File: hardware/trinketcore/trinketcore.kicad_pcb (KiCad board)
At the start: 4 copper layers, 40 x 60 mm, 115 parts, among them J1 USB-C, J4 DISPLAY, J5 I2C OLED, J6 EXPANSION, J7 SPEAKER, J8 QWIIC, Q1 AO3401A, Q2 AO3400A, Q3 AO3400A, Q4 AO3400A, Q5 AO3401A, Q6 AO3400A, Q7 AO3401A, Q8 AO3400A, Q9 AO3400A, SW1 POWER/A, SW2 B, SW3 BOOT, SW4 RESET, U1 USBLC6-2SC6, U2 BQ25173DSGR, U3 TPS3808G01DBVR, U4 TPS63031DSKR, U5 PCF8563T, U6 RP2040, U7 W25Q128JVS, U8 MAX98357A, Y1 32.768kHz, Y2 12MHz

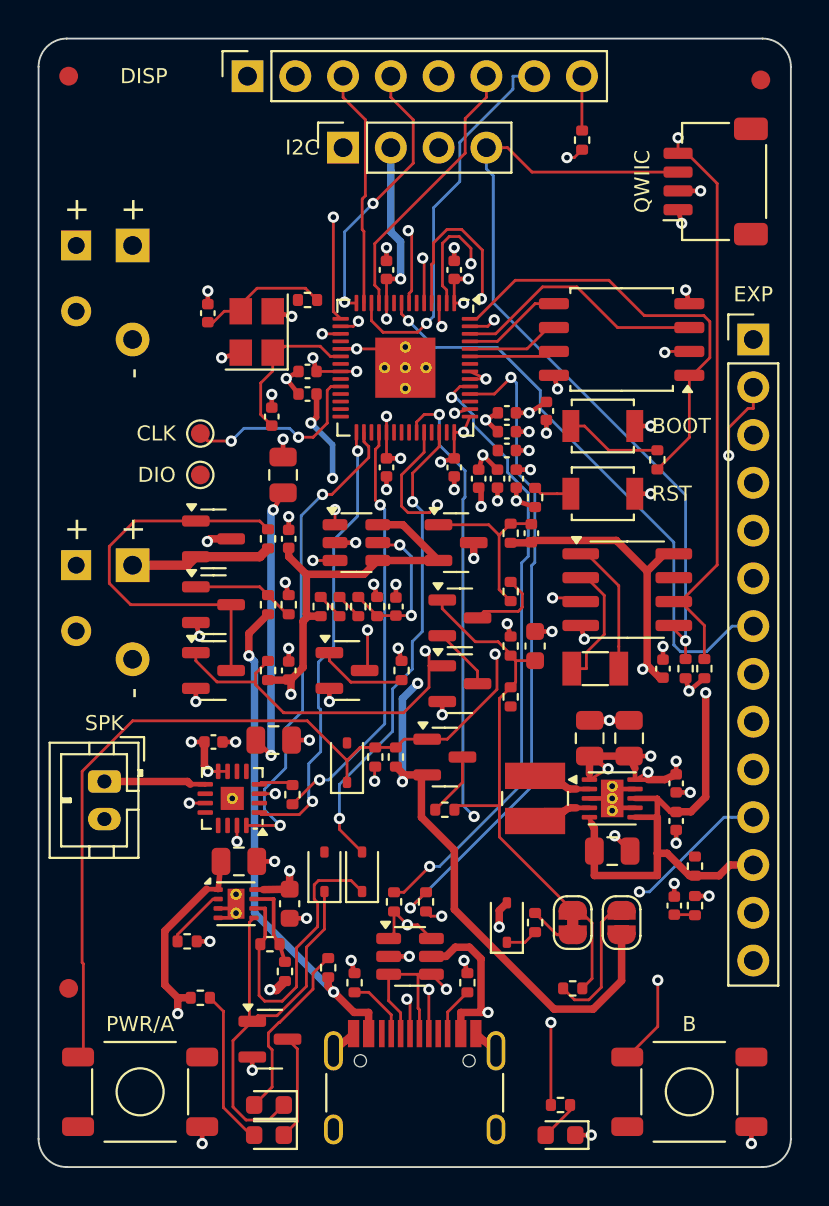
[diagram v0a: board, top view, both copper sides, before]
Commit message: TrinketCore: pin map that routes without crossings (work in progress)
The first autoroute left four connections open. Three of them were at the
RP2040, where the expansion header took GP0..GP7 in the opposite order to the
chip's pins, and USB_DET had to cross GP26/GP27 on the bottom row. The fourth
was the speaker output, hemmed in by a ground via.

- J6 now runs GP7..GP0, GP29, GP28 (pin 1 at the top), matching the pin order.
- Bottom row: CHG GP22, button A GP23, USB_DET GP24, user LED GP25 (unchanged),
  HOLD GP26, VSENSE GP27, J6 analog GP28/GP29. Display DC/CS swap to GP9/GP8.
- The amplifier's ground pins tie into its exposed pad instead of vias, and the
  RP2040 decoupling capacitors share their pins' plane vias.
- route_pcb.py runs a second Freerouting pass on the first pass's result, and
  the grid router falls back to 0.15 mm tracks.

Firmware and docs follow the new pin map. The board is being re-routed; the
board file in this commit is not routed yet.

Co-Authored-By: Claude Opus 5.5 <noreply@anthropic.com>
Claude-Session: https://claude.ai/code/session_01V89YvrQurcttiFbkgcTPH9
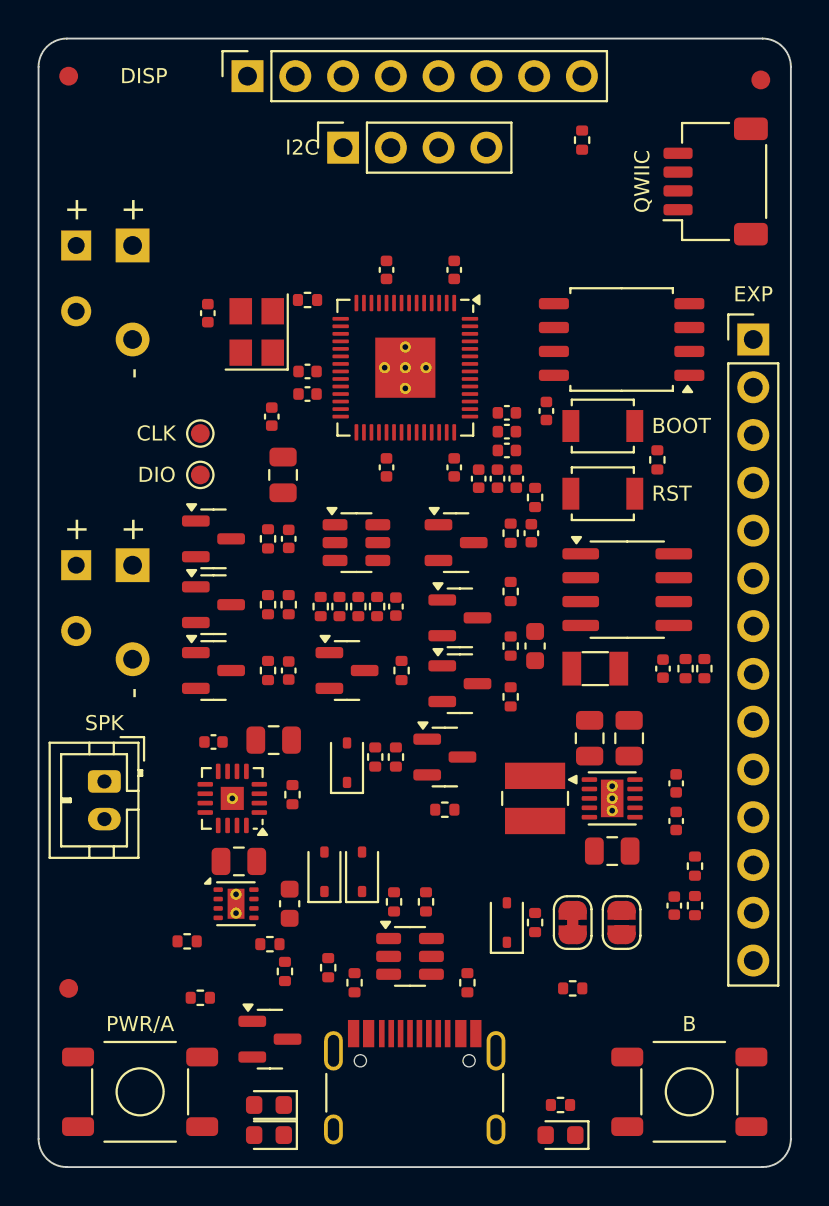
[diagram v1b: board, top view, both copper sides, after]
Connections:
- J6 pad 1: GP0 -> GP7
- J6 pad 10: GP27 -> GP28
- J6 pad 2: GP1 -> GP6
- J6 pad 3: GP2 -> GP5
- J6 pad 4: GP3 -> GP4
- J6 pad 5: GP4 -> GP3
- J6 pad 6: GP5 -> GP2
- J6 pad 7: GP6 -> GP1
- J6 pad 8: GP7 -> GP0
- J6 pad 9: GP26 -> GP29
- U6 pad 11: TFT_DC -> TFT_CS
- U6 pad 12: TFT_CS -> TFT_DC
- U6 pad 34: HOLD -> CHG
- U6 pad 36: CHG -> USB_DET
- U6 pad 38: GP26 -> HOLD
- U6 pad 39: GP27 -> VSENSE
- U6 pad 40: USB_DET -> GP28
- U6 pad 41: VSENSE -> GP29
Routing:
- net 3V3: track 166.3 -> 0.00 mm, vias 27 -> 0
- net VAON: track 99.3 -> 0.00 mm, vias 5 -> 0
- net BTN_B: track 70.1 -> 0.00 mm, vias 2 -> 0
- net VBUS: track 69.6 -> 0.00 mm, vias 5 -> 0
- net VCAP: track 62.6 -> 0.00 mm, vias 2 -> 0
- net GND: track 59.4 -> 0.00 mm, vias 56 -> 0
- net WAKE_N: track 49.9 -> 0.00 mm, vias 2 -> 0
- net GP5: track 44.3 -> 0.00 mm, vias 1 -> 0
- net SCL: track 44.2 -> 0.00 mm, vias 1 -> 0
- net VSYS: track 43.9 -> 0.00 mm, vias 2 -> 0
- net SDA: track 43.4 -> 0.00 mm, vias 1 -> 0
- net USER_LED: track 41.2 -> 0.00 mm, vias 3 -> 0
- net GP3: track 37.5 -> 0.00 mm, vias 1 -> 0
- net USB_DM: track 35.2 -> 0.00 mm, vias 2 -> 0
- net GP26: track 34.1 -> 0.00 mm, vias 1 -> 0
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- removed copper zone on In1.Cu, net GND
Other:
- board text added: "GP28"
- board text added: "GP29"
- board text removed: "GP26"
- board text removed: "GP27"

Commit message: Add e-ink tarot oracle; routing fixes (work in progress)
- firmware/trinketcore/circuitpython/oracle: each press draws a random tarot
  card on a 1.54" SSD1681 e-paper module with a charge icon, then switches the
  board off (the card stays on screen with no power). make_cards.py turns card
  art into dithered 1-bit or black/white/red BMPs with the card's name.
- trinketcore.EPD_BUSY: e-paper BUSY reads on J4's BLK pin (GP13).
- READMEs and the design-method guide cover e-ink wiring and runtimes.
- route_pcb.py: the finisher now sees open connections at SMD pads (the
  report parser only matched "PTH pad"), rips up tracks around boxed-in pads
  and routes them first, and 1V1 uses the default 0.15 mm width so it fits
  between the RP2040's pins. Same parser fix in CapCore's script.
- The SWD test pads are gone (the USB bootloader is in ROM).

The board is being re-routed; the board file in this commit is not routed.

Co-Authored-By: Claude Opus 5.5 <noreply@anthropic.com>
Claude-Session: https://claude.ai/code/session_01V89YvrQurcttiFbkgcTPH9
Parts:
- removed TP1: SWCLK, TestPoint:TestPoint_Pad_D1.0mm
- removed TP2: SWDIO, TestPoint:TestPoint_Pad_D1.0mm
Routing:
- net GND: track 0.00 -> 59.1 mm, vias 0 -> 53
- net 3V3: track 0.00 -> 38.5 mm, vias 0 -> 22
- net VSYS: track 0.00 -> 14.3 mm
- net FB: track 0.00 -> 4.53 mm
- net VCAP: track 0.00 -> 2.88 mm, vias 0 -> 1
- net PG_N: track 0.00 -> 2.59 mm
- net LX2: track 0.00 -> 1.81 mm
- net LX1: track 0.00 -> 1.81 mm
- net VBUS: track 0.00 -> 1.51 mm
- added copper zone on In2.Cu, net 3V3
- added copper zone on B.Cu, net GND
- added copper zone on F.Cu, net GND
- added copper zone on In1.Cu, net GND
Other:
- board text removed: "CLK"
- board text removed: "DIO"

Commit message: TrinketCore: second-pass autoroute session (work in progress)
The grid-router finish, pours and checks follow.

Co-Authored-By: Claude Opus 5.5 <noreply@anthropic.com>
Claude-Session: https://claude.ai/code/session_01V89YvrQurcttiFbkgcTPH9
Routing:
- net 3V3: track 38.5 -> 169.9 mm
- net VAON: track 0.00 -> 91.1 mm, vias 0 -> 6
- net SDA: track 0.00 -> 67.0 mm, vias 0 -> 2
- net VBUS: track 1.51 -> 64.8 mm, vias 0 -> 4
- net SCL: track 0.00 -> 62.5 mm, vias 0 -> 2
- net VCAP: track 2.88 -> 62.7 mm, vias 1 -> 2
- net WAKE_N: track 0.00 -> 51.9 mm, vias 0 -> 4
- net BTN_B: track 0.00 -> 51.6 mm, vias 0 -> 4
- net 1V1: track 0.00 -> 49.1 mm, vias 0 -> 7
- net USER_LED: track 0.00 -> 42.4 mm, vias 0 -> 2
- net USB_DM: track 0.00 -> 39.9 mm, vias 0 -> 2
- net USB_DP: track 0.00 -> 39.9 mm, vias 0 -> 2
- net GP2: track 0.00 -> 37.5 mm, vias 0 -> 1
- net VSENSE: track 0.00 -> 34.7 mm, vias 0 -> 4
- net VSYS: track 14.3 -> 48.4 mm, vias 0 -> 1
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- removed copper zone on In2.Cu, net 3V3
- removed copper zone on B.Cu, net GND
- removed copper zone on F.Cu, net GND

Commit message: TrinketCore: hand-routed crystal corner (work in progress)
The crystal's 1 k resistor now faces the crystal, the XIN capacitor turns so
its signal pad faces the crystal, and pin 22's capacitor moves onto the 3V3
plane to clear the way. XIN and XO are drawn by hand on F.Cu and XOUT hops
over XIN on In2.Cu, so the autorouter no longer has to untangle them.
The board is being re-routed.

Co-Authored-By: Claude Opus 5.5 <noreply@anthropic.com>
Claude-Session: https://claude.ai/code/session_01V89YvrQurcttiFbkgcTPH9
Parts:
- moved C20 6.22 mm to (9.30, 21.4), turned to 90 degrees
- turned C16 to -90 degrees
- turned R31 to 180 degrees
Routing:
- net 3V3: track 169.9 -> 37.9 mm, vias 22 -> 23
- net VAON: track 91.1 -> 0.00 mm, vias 6 -> 0
- net SDA: track 67.0 -> 0.00 mm, vias 2 -> 0
- net VBUS: track 64.8 -> 1.51 mm, vias 4 -> 0
- net SCL: track 62.5 -> 0.00 mm, vias 2 -> 0
- net VCAP: track 62.7 -> 2.88 mm, vias 2 -> 1
- net WAKE_N: track 51.9 -> 0.00 mm, vias 4 -> 0
- net BTN_B: track 51.6 -> 0.00 mm, vias 4 -> 0
- net 1V1: track 49.1 -> 0.00 mm, vias 7 -> 0
- net USER_LED: track 42.4 -> 0.00 mm, vias 2 -> 0
- net USB_DM: track 39.9 -> 0.00 mm, vias 2 -> 0
- net USB_DP: track 39.9 -> 0.00 mm, vias 2 -> 0
- net GP2: track 37.5 -> 0.00 mm, vias 1 -> 0
- net VSENSE: track 34.7 -> 0.00 mm, vias 4 -> 0
- net VSYS: track 48.4 -> 14.3 mm, vias 1 -> 0
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- added copper zone on In2.Cu, net 3V3
- added copper zone on B.Cu, net GND
- added copper zone on F.Cu, net GND

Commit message: TrinketCore: second-pass session for the new crystal corner (work in progress)
Co-Authored-By: Claude Opus 5.5 <noreply@anthropic.com>
Claude-Session: https://claude.ai/code/session_01V89YvrQurcttiFbkgcTPH9
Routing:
- net 3V3: track 37.9 -> 168.2 mm
- net VAON: track 0.00 -> 94.2 mm, vias 0 -> 4
- net BTN_B: track 0.00 -> 66.5 mm, vias 0 -> 3
- net SCL: track 0.00 -> 64.1 mm, vias 0 -> 2
- net SDA: track 0.00 -> 60.8 mm, vias 0 -> 4
- net WAKE_N: track 0.00 -> 59.8 mm, vias 0 -> 3
- net VCAP: track 2.88 -> 61.3 mm, vias 1 -> 2
- net VBUS: track 1.51 -> 56.9 mm, vias 0 -> 6
- net UVLO_OK: track 0.00 -> 42.2 mm, vias 0 -> 2
- net USER_LED: track 0.00 -> 40.0 mm, vias 0 -> 2
- net VSENSE: track 0.00 -> 35.8 mm, vias 0 -> 2
- net VSYS: track 14.3 -> 48.1 mm, vias 0 -> 1
- net GP28: track 0.00 -> 30.9 mm, vias 0 -> 1
- net GP2: track 0.00 -> 30.4 mm, vias 0 -> 1
- net EN_SYS: track 0.00 -> 29.9 mm
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- removed copper zone on In2.Cu, net 3V3
- removed copper zone on B.Cu, net GND
- removed copper zone on F.Cu, net GND

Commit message: TrinketCore: free the RP2040's top escape lanes (work in progress)
C18 and C19, the decoupling capacitors for pins 1 and 10, move to the
chip's corners on their own plane vias, so the GPIO and display tracks can
leave the top row in parallel. The second Freerouting pass gets 40 passes
and the grid router a wider rip-up radius. The board is being re-routed.

Co-Authored-By: Claude Opus 5.5 <noreply@anthropic.com>
Claude-Session: https://claude.ai/code/session_01V89YvrQurcttiFbkgcTPH9
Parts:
- moved C19 3.37 mm to (15.2, 11.6)
- moved C18 1.71 mm to (23.7, 12.9), turned to 0 degrees
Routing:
- net 3V3: track 168.2 -> 36.7 mm, vias 23 -> 25
- net VAON: track 94.2 -> 0.00 mm, vias 4 -> 0
- net BTN_B: track 66.5 -> 0.00 mm, vias 3 -> 0
- net SCL: track 64.1 -> 0.00 mm, vias 2 -> 0
- net SDA: track 60.8 -> 0.00 mm, vias 4 -> 0
- net WAKE_N: track 59.8 -> 0.00 mm, vias 3 -> 0
- net VCAP: track 61.3 -> 2.88 mm, vias 2 -> 1
- net VBUS: track 56.9 -> 1.51 mm, vias 6 -> 0
- net UVLO_OK: track 42.2 -> 0.00 mm, vias 2 -> 0
- net USER_LED: track 40.0 -> 0.00 mm, vias 2 -> 0
- net VSENSE: track 35.8 -> 0.00 mm, vias 2 -> 0
- net VSYS: track 48.1 -> 14.3 mm, vias 1 -> 0
- net GP28: track 30.9 -> 0.00 mm, vias 1 -> 0
- net GP2: track 30.4 -> 0.00 mm, vias 1 -> 0
- net EN_SYS: track 29.9 -> 0.00 mm
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- added copper zone on In2.Cu, net 3V3
- added copper zone on B.Cu, net GND
- added copper zone on F.Cu, net GND

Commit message: TrinketCore: second-pass session, free escape lanes (work in progress)
Co-Authored-By: Claude Opus 5.5 <noreply@anthropic.com>
Claude-Session: https://claude.ai/code/session_01V89YvrQurcttiFbkgcTPH9
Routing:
- net 3V3: track 36.7 -> 167.7 mm
- net VAON: track 0.00 -> 109.1 mm, vias 0 -> 5
- net SDA: track 0.00 -> 66.6 mm, vias 0 -> 3
- net SCL: track 0.00 -> 62.7 mm, vias 0 -> 2
- net VBUS: track 1.51 -> 63.7 mm, vias 0 -> 4
- net VCAP: track 2.88 -> 62.7 mm, vias 1 -> 2
- net BTN_B: track 0.00 -> 51.8 mm, vias 0 -> 3
- net 1V1: track 0.00 -> 47.9 mm, vias 0 -> 6
- net USER_LED: track 0.00 -> 46.4 mm, vias 0 -> 3
- net CHG: track 0.00 -> 44.8 mm, vias 0 -> 2
- net WAKE_N: track 0.00 -> 41.7 mm, vias 0 -> 4
- net USB_DP: track 0.00 -> 37.9 mm, vias 0 -> 2
- net VSENSE: track 0.00 -> 35.9 mm, vias 0 -> 2
- net I2S_BCLK: track 0.00 -> 34.6 mm, vias 0 -> 3
- net GP28: track 0.00 -> 33.4 mm, vias 0 -> 2
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- removed copper zone on In2.Cu, net 3V3
- removed copper zone on B.Cu, net GND
- removed copper zone on F.Cu, net GND

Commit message: TrinketCore: fully routed board and PCBWay files
The board now routes completely: two Freerouting passes, then the grid
router closes the last three connections (LED_A and the speaker pair).
KiCad DRC with PCBWay's limits reports no errors and no unconnected items,
only the cosmetic USB-C footprint warning, and the schematic and PCB match
netlist.py pin for pin (378 pins).

- fab/: Gerbers + drill (zip for upload), PCBWay BOMs for the LIC and EDLC
  builds (44 lines, 102 parts), pick-and-place, assembly drawings, parts list.
- trinketcore-schematic.pdf and board renders in docs/images.
- check_netlist.py treats unnetted mechanical pads (J8's mounting tabs) as a
  note instead of a problem.
- README: verification status. The board has not been built yet.

Co-Authored-By: Claude Opus 5.5 <noreply@anthropic.com>
Claude-Session: https://claude.ai/code/session_01V89YvrQurcttiFbkgcTPH9
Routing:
- added copper zone on In2.Cu, net 3V3
- added copper zone on B.Cu, net GND
- added copper zone on F.Cu, net GND
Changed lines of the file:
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@@
   (segment (start 28.9 4.89) (end 28.89 4.88) (width 0.15) (layer "F.Cu") (net 89))
   (segment (start 28.89 4.88) (end 28.89 2) (width 0.15) (layer "F.Cu") (net 89))
+  (zone (net 1) (net_name "GND") (layer "F.Cu") (hatch edge 0.5)
+    (connect_pads (clearance 0.2))
+    (min_thickness 0.2) (filled_areas_thickness no)
+    (fill yes (thermal_gap 0.25) (thermal_bridge_width 0.3))
+    (polygon
+      (pts
+        (xy 0.3 0.3)
+        (xy 39.7 0.3)
+        (xy 39.7 59.7)
+        (xy 0.3 59.7)
+      )
+    )
+  )
   (zone (net 0) (net_name "") (layer "F.Cu") (hatch edge 0.5)
     (connect_pads (clearance 0))
@@
     (connect_pads (clearance 0.2))
     (min_thickness 0.2) (filled_areas_thickness no)
+    (fill yes (thermal_gap 0.25) (thermal_bridge_width 0.3))
+    (polygon
+      (pts
+        (xy 0.3 0.3)
+        (xy 39.7 0.3)
+        (xy 39.7 59.7)
+        (xy 0.3 59.7)
+      )
+    )
+  )
+  (zone (net 41) (net_name "3V3") (layer "In2.Cu") (hatch edge 0.5)
+    (connect_pads (clearance 0.2))
+    (min_thickness 0.2) (filled_areas_thickness no)
+    (fill yes (thermal_gap 0.25) (thermal_bridge_width 0.3))
+    (polygon
+      (pts
+        (xy 0.3 0.3)
+        (xy 39.7 0.3)
+        (xy 39.7 59.7)
+        (xy 0.3 59.7)
+      )
+    )
+  )
+  (zone (net 1) (net_name "GND") (layer "B.Cu") (hatch edge 0.5)
+    (connect_pads (clearance 0.2))
+    (min_thickness 0.2) (filled_areas_thickness no)
